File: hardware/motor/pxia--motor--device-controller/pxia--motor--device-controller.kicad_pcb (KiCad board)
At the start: 2 copper layers, 54 x 42 mm, 14 parts, among them J1 IDC(>ENCODER), J2 JST-PHD(>SMCI12(X12)), J3 JST-PHD(>SMCI12(X11)), J4 Screw_Terminal_01x02, J5 RJ45, J6 RJ45, U1 LM7805_TO220

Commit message: updated PCBs
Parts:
- moved J4 1.00 mm to (144.0, 133.5)
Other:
- board text added: "24V"
- board text added: "5V"
- board text added: "GND"
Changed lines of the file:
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@@
   )
   (footprint "TerminalBlock:TerminalBlock_bornier-2_P5.08mm" (layer "F.Cu")
-    (at 143 133.54 90)
+    (at 144 133.54 90)
     (descr "simple 2-pin terminal block, pitch 5.08mm, revamped version of bornier2")
     (tags "terminal block bornier2")
@@
       (effects (font (size 1 1) (thickness 0.15)))
     )
-    (fp_line (start 2.5 14.075736) (end 2.2 14.5) (layer "F.SilkS") (width 0.12))
     (fp_line (start 4.31 5.15) (end 4.31 4.85) (layer "F.SilkS") (width 0.12))
     (fp_line (start 4.31 10.15) (end 4.31 9.85) (layer "F.SilkS") (width 0.12))
@@
     (fp_line (start 4.31 -1.83) (end 4.31 14.33) (layer "F.SilkS") (width 0.12))
     (fp_line (start 4.31 9.85) (end 3.61 9.85) (layer "F.SilkS") (width 0.12))
-    (fp_line (start 2.8 14.5) (end 2.5 14.075736) (layer "F.SilkS") (width 0.12))
     (fp_line (start 4.31 7.35) (end 3.61 7.35) (layer "F.SilkS") (width 0.12))
     (fp_line (start 4.31 12.65) (end 4.31 12.35) (layer "F.SilkS") (width 0.12))
-    (fp_line (start 2.2 14.5) (end 2.8 14.5) (layer "F.SilkS") (width 0.12))
     (fp_line (start -1.35 -2.22) (end -1.35 14.72) (layer "F.CrtYd") (width 0.05))
     (fp_line (start 13.38 14.72) (end 13.38 -2.22) (layer "F.CrtYd") (width 0.05))
@@
     )
   )
-  (gr_line (start 104.5 100) (end 100 104.5) (layer "F.SilkS") (width 0.1))
-  (gr_line (start 104.5 142) (end 100 137.5) (layer "F.SilkS") (width 0.1))
-  (gr_line (start 141.986362 104.5) (end 137.486362 100) (layer "F.SilkS") (width 0.1))
-  (gr_line (start 137.5 142) (end 142 137.5) (layer "F.SilkS") (width 0.1))
+  (gr_circle (center 138.5 138) (end 138.75 138) (layer "F.SilkS") (width 0.25) (fill none))
   (gr_line (start 143.5 142) (end 148 137.5) (layer "Edge.Cuts") (width 0.1))
   (gr_line (start 98.5 142) (end 94 137.5) (layer "Edge.Cuts") (width 0.1))
@@
   (gr_line (start 98.5 100) (end 94 104.5) (layer "Edge.Cuts") (width 0.1))
   (gr_line (start 148 137.5) (end 148 104.5) (layer "Edge.Cuts") (width 0.1))
+  (gr_text "GND" (at 110.424264 133) (layer "F.SilkS")
+    (effects (font (size 0.5 0.5) (thickness 0.1)) (justify right))
+  )
+  (gr_text "5V" (at 126 130.5) (layer "F.SilkS")
+    (effects (font (size 0.5 0.5) (thickness 0.1)) (justify left))
+  )
+  (gr_text "GND" (at 139.5 133.5) (layer "F.SilkS")
+    (effects (font (size 0.5 0.5) (thickness 0.1)) (justify right))
+  )
+  (gr_text "24V" (at 139.5 128.5) (layer "F.SilkS")
+    (effects (font (size 0.5 0.5) (thickness 0.1)) (justify right))
+  )
   (dimension (type aligned) (layer "F.Fab")
     (pts (xy 94 137.5) (xy 148 137.5))

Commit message: finished routing
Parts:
- moved J4 1.00 mm to (144.0, 134.5)
- moved J6 0.50 mm to (134.9, 121.8)
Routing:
- net +24V: track 0.00 -> 78.7 mm, vias 0 -> 1
- net /OUTPUT_3: track 0.00 -> 71.2 mm, vias 0 -> 2
- net /OUTPUT_2: track 0.00 -> 71.1 mm, vias 0 -> 1
- net /OUTPUT_1: track 0.00 -> 63.4 mm, vias 0 -> 1
- net /TX-: track 0.00 -> 58.2 mm, vias 0 -> 1
- net /TX+: track 0.00 -> 52.5 mm, vias 0 -> 1
- net /RX-: track 0.00 -> 47.8 mm, vias 0 -> 2
- net GND: track 0.00 -> 43.9 mm, vias 0 -> 2
- net /RX+: track 0.00 -> 43.3 mm
- net Net-(J5-Pad3): track 0.00 -> 37.6 mm, vias 0 -> 3
- net /INPUT_5: track 0.00 -> 31.6 mm, vias 0 -> 1
- net /ANALOG_IN: track 0.00 -> 30.5 mm, vias 0 -> 1
- net Net-(J5-Pad5): track 0.00 -> 28.9 mm, vias 0 -> 2
- net /INPUT_6: track 0.00 -> 28.3 mm
- net /INPUT_1: track 0.00 -> 27.9 mm
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- added copper zone on F.Cu, net (none)
- added copper zone on B.Cu, net GND

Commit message: added PicoW, finished PCB layout
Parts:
- J1: value IDC(>ENCODER) -> IDC(>ENC)
- J4: value Screw_Terminal_01x02 -> PWR_SUPPLY
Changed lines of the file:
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@@
       (effects (font (size 1 1) (thickness 0.15)))
     )
-    (fp_text value "Screw_Terminal_01x02" (at 2.54 5.08 90) (layer "F.Fab")
+    (fp_text value "PWR_SUPPLY" (at 2.54 5.08 90) (layer "F.Fab")
       (effects (font (size 1 1) (thickness 0.15)))
     )
@@
       (effects (font (size 1 1) (thickness 0.15)))
     )
-    (fp_text value "IDC(>ENCODER)" (at 6.5 6) (layer "F.Fab")
-      (effects (font (size 1 1) (thickness 0.15)))
-    )
+    (fp_text value "IDC(>ENC)" (at 6.5 6) (layer "F.Fab")
+      (effects (font (size 1 1) (thickness 0.15)))
+    )

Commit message: cleaned up, production ready
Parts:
- J4: footprint TerminalBlock:TerminalBlock_bornier-2_P5.08mm -> TerminalBlock_MetzConnect:TerminalBlock_MetzConnect_Type055_RT01502HDWU_1x02_P5.00mm_Horizontal
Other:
- board size 54 x 42 mm -> 56 x 42 mm

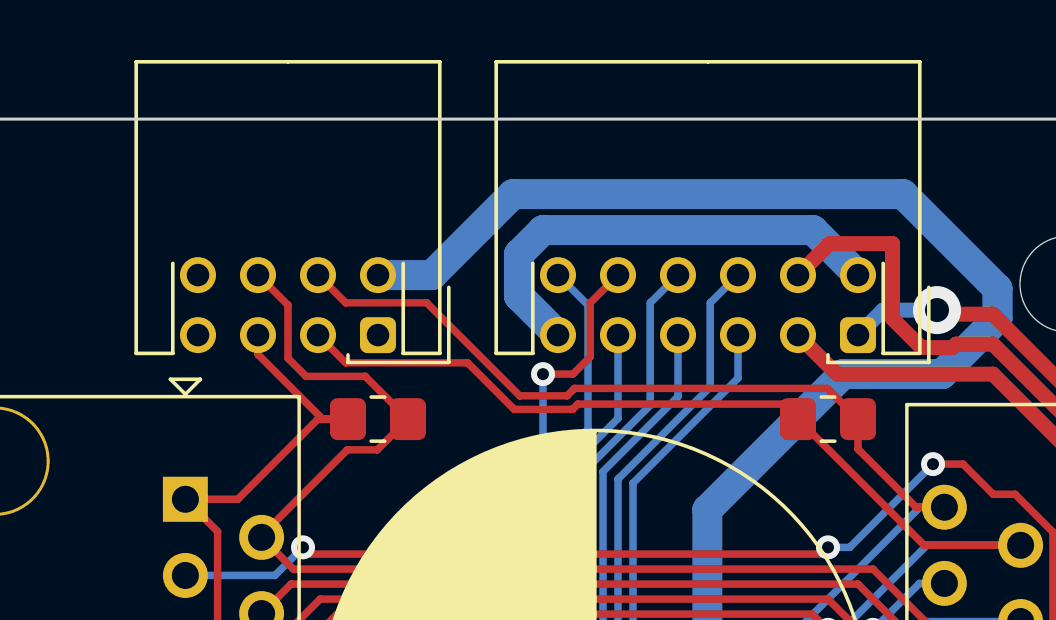
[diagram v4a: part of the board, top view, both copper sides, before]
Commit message: updated documentation, fixed wrong wiring
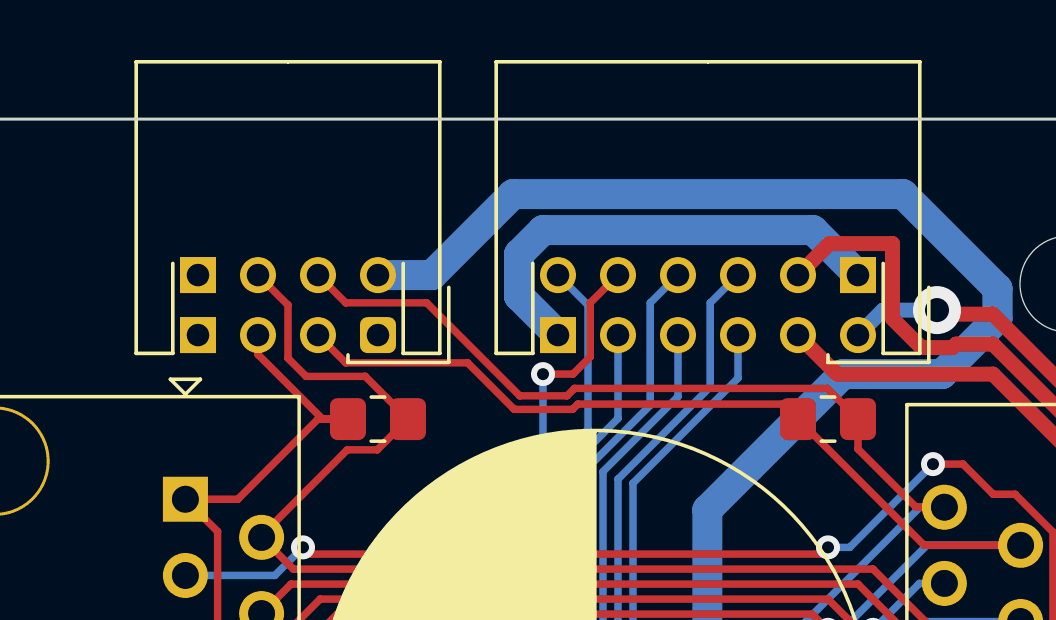
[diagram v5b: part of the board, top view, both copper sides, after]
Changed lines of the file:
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@@
     (pad "6" thru_hole circle (at 4 2 180) (size 1.2 1.2) (drill 0.75) (layers *.Cu *.Mask)
       (net 15 "/RX+") (pinfunction "Pin_6") (pintype "passive"))
-    (pad "7" thru_hole circle (at 6 0 180) (size 1.2 1.2) (drill 0.75) (layers *.Cu *.Mask)
+    (pad "7" thru_hole rect (at 6 0 180) (size 1.2 1.2) (drill 0.75) (layers *.Cu *.Mask)
       (net 2 "GND") (pinfunction "Pin_7") (pintype "passive"))
-    (pad "8" thru_hole circle (at 6 2 180) (size 1.2 1.2) (drill 0.75) (layers *.Cu *.Mask)
+    (pad "8" thru_hole rect (at 6 2 180) (size 1.2 1.2) (drill 0.75) (layers *.Cu *.Mask)
       (net 2 "GND") (pinfunction "Pin_8") (pintype "passive"))
     (model "${KICAD6_3DMODEL_DIR}/Connector_JST.3dshapes/JST_PHD_S8B-PHDSS_2x04_P2.00mm_Horizontal.wrl"
@@
     (fp_line (start -1.95 9) (end -1.95 -0.5) (layer "F.Fab") (width 0.1))
     (fp_line (start -0.242893 0) (end -0.95 0.5) (layer "F.Fab") (width 0.1))
-    (pad "1" thru_hole roundrect (at 0 0 180) (size 1.2 1.2) (drill 0.75) (layers *.Cu *.Mask) (roundrect_rratio 0.2083333333)
+    (pad "1" thru_hole circle (at 0 0 180) (size 1.2 1.2) (drill 0.75) (layers *.Cu *.Mask)
       (net 13 "/OUTPUT_3") (pinfunction "Pin_1") (pintype "passive"))
-    (pad "2" thru_hole circle (at 0 2 180) (size 1.2 1.2) (drill 0.75) (layers *.Cu *.Mask)
+    (pad "2" thru_hole rect (at 0 2 180) (size 1.2 1.2) (drill 0.75) (layers *.Cu *.Mask)
       (net 2 "GND") (pinfunction "Pin_2") (pintype "passive"))
     (pad "3" thru_hole circle (at 2 0 180) (size 1.2 1.2) (drill 0.75) (layers *.Cu *.Mask)
@@
     (pad "10" thru_hole circle (at 8 2 180) (size 1.2 1.2) (drill 0.75) (layers *.Cu *.Mask)
       (net 6 "/INPUT_3") (pinfunction "Pin_10") (pintype "passive"))
-    (pad "11" thru_hole circle (at 10 0 180) (size 1.2 1.2) (drill 0.75) (layers *.Cu *.Mask)
+    (pad "11" thru_hole rect (at 10 0 180) (size 1.2 1.2) (drill 0.75) (layers *.Cu *.Mask)
       (net 2 "GND") (pinfunction "Pin_11") (pintype "passive"))
     (pad "12" thru_hole circle (at 10 2 180) (size 1.2 1.2) (drill 0.75) (layers *.Cu *.Mask)
